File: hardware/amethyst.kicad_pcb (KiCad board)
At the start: 2 copper layers, 192 parts, among them J1 Conn_01x02_Pin, J2 USB_C_Receptacle_USB2.0_16P, SW1 SW_Push, SW10 SW_Push, SW11 SW_Push, SW12 SW_Push, SW13 SW_Push, SW14 SW_Push, SW15 SW_Push, SW16 SW_Push, SW17 SW_Push, SW18 SW_Push, SW19 SW_Push, SW2 SW_Push, SW20 SW_Push, SW21 SW_Push, SW22 SW_Push, SW23 SW_Push, SW24 SW_Push, SW25 SW_Push, SW26 SW_Push, SW27 SW_Push, SW28 SW_Push, SW29 SW_Push, SW3 SW_Push, SW30 SW_Push, SW31 SW_Push, SW32 SW_Push, SW33 SW_Push, SW34 SW_Push, SW35 SW_Push, SW36 SW_Push, SW37 SW_Push, SW38 SW_Push, SW39 SW_Push, SW4 SW_Push, SW40 SW_Push, SW41 SW_Push, SW42 SW_Push, SW43 SW_Push, SW44 SW_Push, SW45 SW_Push, SW46 SW_Push, SW47 SW_Push, SW48 SW_Push, SW49 SW_Push, SW5 SW_Push, SW50 SW_Push, SW51 SW_Push, SW52 SW_Push, SW53 SW_Push, SW54 SW_Push, SW55 SW_Push, SW56 SW_Push, SW57 SW_Push, SW58 SW_Push, SW59 SW_Push, SW6 SW_Push, SW60 SW_Push, SW61 SW_Push, SW62 SW_Push, SW63 SW_Push, SW64 SW_Push, SW65 SW_Push, SW66 SW_Push, SW67 SW_Push, SW68 SW_Push, SW69 SW_Push, SW7 SW_Push, SW70 SW_Push, SW71 SW_Push, SW72 SW_Push, SW73 SW_Push, SW74 SW_Push, SW75 SW_Push, SW76 SW_Push, SW77 SW_Push, SW78 SW_Push, SW79 SW_Push, SW8 SW_Push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

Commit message: PCB Routing
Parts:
- removed C1, C2: C, Capacitor_SMD:C_0402_1005Metric
- removed C10, C11, C12, C13, C14, C3, C4, C5, C6, C7, C8: 100n, Capacitor_SMD:C_0402_1005Metric
- removed C9: 1u, Capacitor_SMD:C_0402_1005Metric
- removed J1: Conn_01x02_Pin, Connector_PinHeader_1.00mm:PinHeader_1x02_P1.00mm_Vertical
- removed J2: USB_C_Receptacle_USB2.0_16P, Connector_USB:USB_C_Receptacle_XKB_U262-16XN-4BVC11
- removed R1, R2: 5.1k, Resistor_SMD:R_0402_1005Metric
- removed R3: 1k, Resistor_SMD:R_0402_1005Metric
- removed R4, R5: 27, Resistor_SMD:R_0402_1005Metric
- removed U1: RP2040, Package_DFN_QFN:QFN-56-1EP_7x7mm_P0.4mm_EP3.2x3.2mm
- removed U2: W25Q128JVS, Package_SO:SOIC-8_5.3x5.3mm_P1.27mm
- removed Y1: Crystal_GND24_Small, Crystal:Crystal_SMD_3225-4Pin_3.2x2.5mm
- D1, D10, D11, D12, D13, D14, D15, D16, D17, D18, D19, D2, D20, D21, D22, D23, D24, D25, D26, D27, D28, D29, D3, D30, D31, D32, D33, D34, D35, D36, D37, D38, D39, D4, D40, D41, D42, D43, D44, D45, D46, D47, D48, D49, D5, D50, D51, D52, D53, D54, D55, D56, D57, D58, D59, D6, D60, D61, D62, D63, D64, D65, D66, D67, D68, D69, D7, D70, D71, D72, D73, D74, D75, D76, D77, D78, D79, D8, D80, D81, D82, D83, D84, D9: moved to B.Cu
- moved D75 299.2 mm to (71.4, 161.9), turned to 90 degrees
- moved D17 291.3 mm to (69.1, 85.7), turned to 90 degrees
- moved D47 289.6 mm to (76.2, 123.8), turned to 90 degrees
- moved D32 289.2 mm to (73.8, 104.8), turned to 90 degrees
- moved D1 288.0 mm to (69.1, 66.7), turned to 90 degrees
- moved D61 285.1 mm to (81.0, 142.9), turned to 90 degrees
- moved D76 275.7 mm to (95.2, 161.9), turned to 90 degrees
- moved D18 274.9 mm to (88.1, 85.7), turned to 90 degrees
- moved D2 271.9 mm to (88.1, 66.7), turned to 90 degrees
- moved D33 268.0 mm to (97.6, 104.8), turned to 90 degrees
- moved D48 265.8 mm to (102.4, 123.8), turned to 90 degrees
- moved D19 258.9 mm to (107.2, 85.7), turned to 90 degrees
- moved D3 256.2 mm to (107.2, 66.7), turned to 90 degrees
- moved D62 254.9 mm to (111.9, 142.9), turned to 90 degrees
- moved D77 252.4 mm to (119.1, 161.9), turned to 90 degrees
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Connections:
- SW78 pad 1: C7 -> C6
- SW79 pad 1: C11 -> C10
- SW80 pad 1: C12 -> C11
- SW81 pad 1: C13 -> C12
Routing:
- net R2: track 0.00 -> 288.5 mm
- net R6: track 0.00 -> 287.1 mm
- net R1: track 0.00 -> 285.8 mm
- net R4: track 0.00 -> 281.3 mm
- net R3: track 0.00 -> 281.0 mm
- net R5: track 0.00 -> 275.2 mm
- net C2: track 0.00 -> 114.7 mm
- net C14: track 0.00 -> 114.3 mm
- net C3: track 0.00 -> 110.4 mm
- net C11: track 0.00 -> 107.4 mm
- net C10: track 0.00 -> 107.4 mm
- net C6: track 0.00 -> 106.3 mm
- net C1: track 0.00 -> 105.1 mm
- net C12: track 0.00 -> 103.3 mm
- net C15: track 0.00 -> 101.3 mm
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
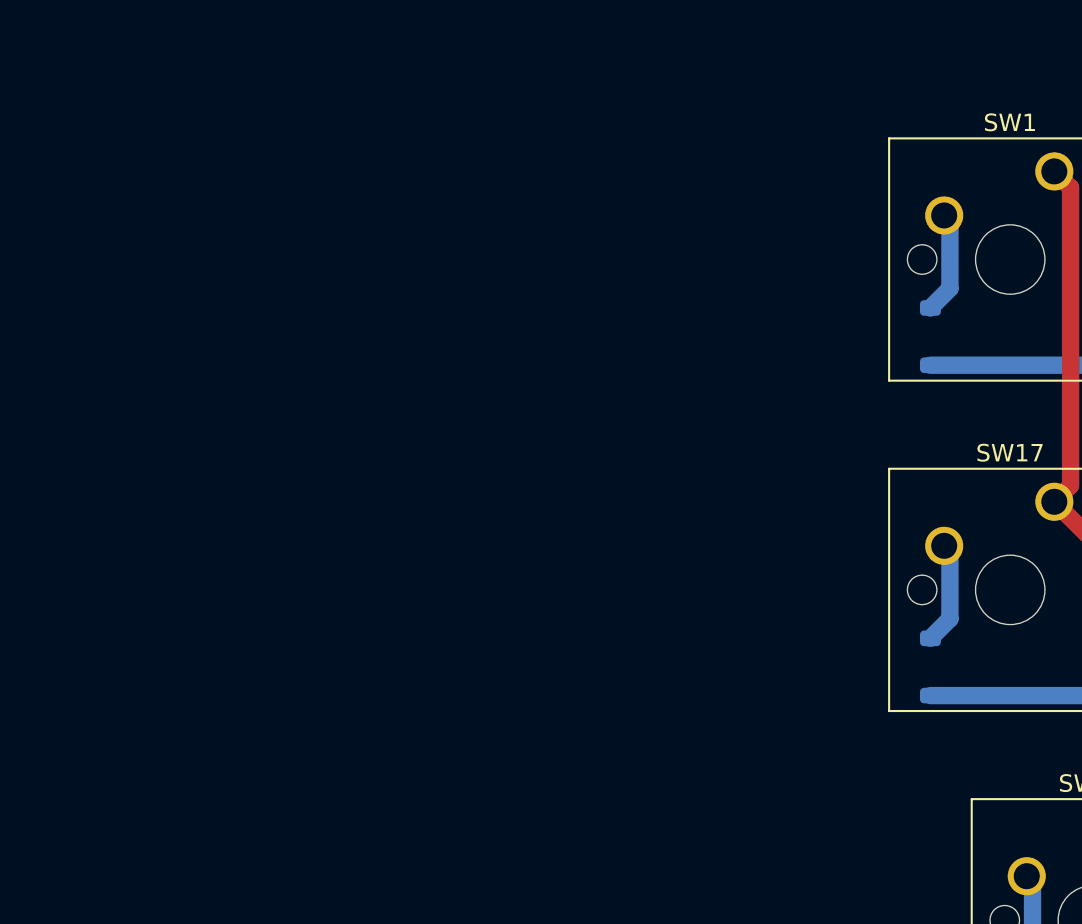
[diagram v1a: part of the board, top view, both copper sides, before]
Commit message: Power circuitry and nrf52840 circuitry
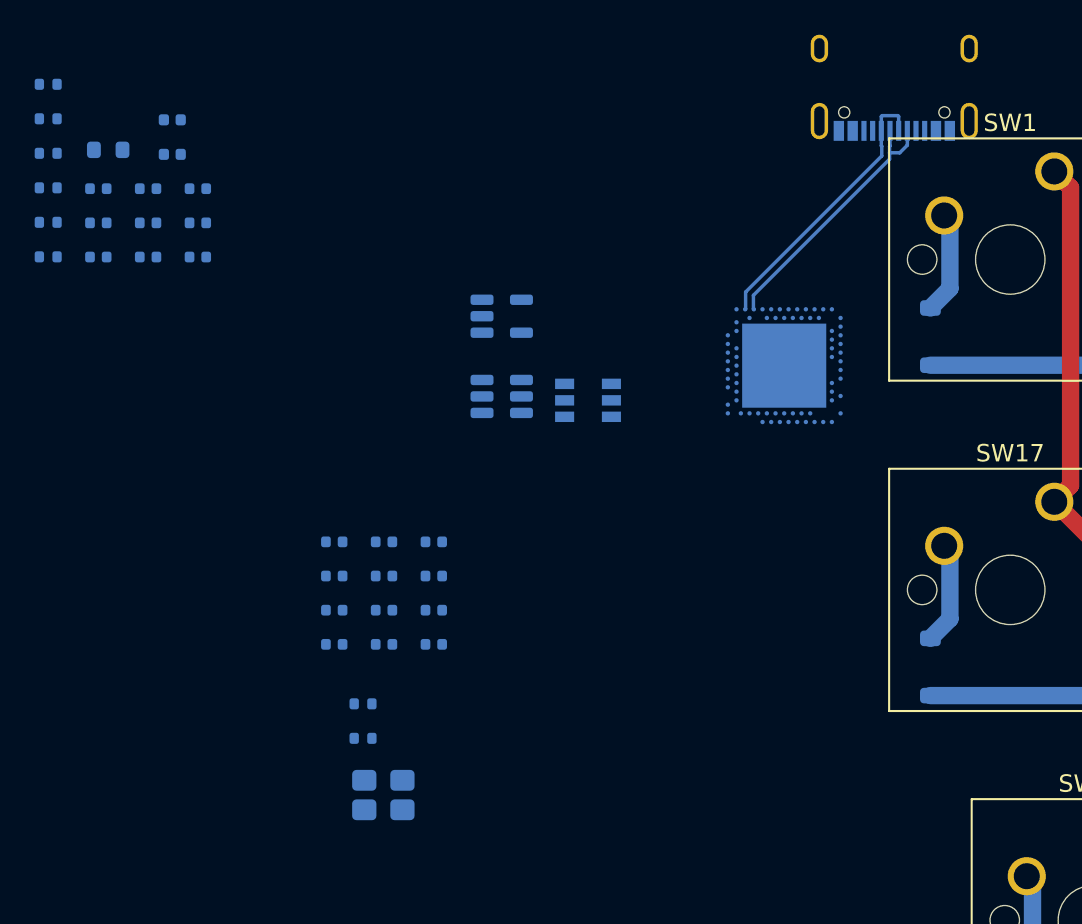
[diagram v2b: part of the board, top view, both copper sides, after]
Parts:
- added C1: C, Capacitor_SMD:C_0402_1005Metric, B.Cu at (34.7, 84.4)
- added C10: 100p, Capacitor_SMD:C_0402_1005Metric, B.Cu at (40.4, 82.5)
- added C11: 4.7u, Capacitor_SMD:C_0402_1005Metric, B.Cu at (40.4, 80.5)
- added C12: 100n, Capacitor_SMD:C_0402_1005Metric, B.Cu at (21.1, 60.1)
- added C12: 4.7u, Capacitor_SMD:C_0402_1005Metric, B.Cu at (40.4, 78.5)
- added C13: 1u, Capacitor_SMD:C_0402_1005Metric, B.Cu at (21.1, 58.1)
- added C14: 1u, Capacitor_SMD:C_0402_1005Metric, B.Cu at (23.9, 62.1)
- added C15: 47n, Capacitor_SMD:C_0402_1005Metric, B.Cu at (23.9, 60.1)
- added C16: 100n, Capacitor_SMD:C_0402_1005Metric, B.Cu at (23.9, 58.1)
- added C17: 100n, Capacitor_SMD:C_0402_1005Metric, B.Cu at (26.8, 62.1)
- added C18: 850p, Capacitor_SMD:C_0402_1005Metric, B.Cu at (26.8, 60.1)
- added C19: 100n, Capacitor_SMD:C_0402_1005Metric, B.Cu at (26.8, 58.1)
- added C2: C, Capacitor_SMD:C_0402_1005Metric, B.Cu at (34.7, 82.5)
- added C3: 100n, Capacitor_SMD:C_0402_1005Metric, B.Cu at (34.7, 80.5)
- added C4: 100n, Capacitor_SMD:C_0402_1005Metric, B.Cu at (34.7, 78.5)
- added C4: 100n, Capacitor_SMD:C_0402_1005Metric, B.Cu at (21.1, 62.1)
- added C5: 100n, Capacitor_SMD:C_0402_1005Metric, B.Cu at (37.5, 84.4)
- added C6: 100n, Capacitor_SMD:C_0402_1005Metric, B.Cu at (37.5, 82.5)
- added C7: 100n, Capacitor_SMD:C_0402_1005Metric, B.Cu at (37.5, 80.5)
- added C8: 100n, Capacitor_SMD:C_0402_1005Metric, B.Cu at (37.5, 78.5)
- added C9: 100n, Capacitor_SMD:C_0402_1005Metric, B.Cu at (40.4, 84.4)
- added D85: LED, LED_SMD:LED_0402_1005Metric, B.Cu at (25.3, 56.2)
- added D86: LED, LED_SMD:LED_0402_1005Metric, B.Cu at (25.3, 54.2)
- added FB1: FerriteBead_Small, Resistor_SMD:R_0603_1608Metric, B.Cu at (21.6, 55.9)
- added J2: USB_C_Receptacle_USB2.0_16P, Connector_USB:USB_C_Receptacle_XKB_U262-16XN-4BVC11, B.Cu at (67.0, 51.1)
- added Q1: FS8205A_C2830320, easyeda2kicad:SOT-23-6_L2.9-W1.6-P0.95-LS2.8-BR, B.Cu at (49.3, 70.3)
- added R1: 5.1k, Resistor_SMD:R_0402_1005Metric, B.Cu at (36.3, 89.8)
- added R2: 5.1k, Resistor_SMD:R_0402_1005Metric, B.Cu at (36.3, 87.8)
- added R3: 100, Resistor_SMD:R_0402_1005Metric, B.Cu at (18.2, 62.1)
- added R4: 1k, Resistor_SMD:R_0402_1005Metric, B.Cu at (18.2, 60.1)
- added R5: 1k, Resistor_SMD:R_0402_1005Metric, B.Cu at (18.2, 58.1)
- added R6: 1k, Resistor_SMD:R_0402_1005Metric, B.Cu at (18.2, 56.1)
- added R7: R, Resistor_SMD:R_0402_1005Metric, B.Cu at (18.2, 54.1)
- added R8: R, Resistor_SMD:R_0402_1005Metric, B.Cu at (18.2, 52.1)
- added U1: nRF52840, Package_DFN_QFN:Nordic_AQFN-73-1EP_7x7mm_P0.5mm, B.Cu at (60.6, 68.3)
- added U2: DW01A, Package_TO_SOT_SMD:SOT-23-6, B.Cu at (44.3, 70.1)
- added U3: MCP73831-2-OT, Package_TO_SOT_SMD:SOT-23-5, B.Cu at (44.3, 65.5)
- added Y1: Crystal_GND24_Small, Crystal:Crystal_SMD_3225-4Pin_3.2x2.5mm, B.Cu at (37.5, 93.1)
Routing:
- net D-: track 0.00 -> 16.3 mm
- net D+: track 0.00 -> 15.6 mm

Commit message: Routing
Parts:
- removed the C12 at (21.1, 60.1)
- removed the C12 at (40.4, 78.5)
- removed the C4 at (34.7, 78.5)
- removed the C4 at (21.1, 62.1)
- removed Q1: FS8205A_C2830320, easyeda2kicad:SOT-23-6_L2.9-W1.6-P0.95-LS2.8-BR
- removed R7: R, Resistor_SMD:R_0402_1005Metric
- removed U3: MCP73831-2-OT, Package_TO_SOT_SMD:SOT-23-5
- added BT1: Battery_Cell, Connector_JST:JST_EH_B2B-EH-A_1x02_P2.50mm_Vertical, B.Cu at (69.0, 98.0)
- added C12: 100n, Capacitor_SMD:C_0402_1005Metric, B.Cu at (48.2, 67.0)
- added C20: 10u, Capacitor_SMD:C_0805_2012Metric, B.Cu at (39.5, 69.9)
- added C21: 100n, Capacitor_SMD:C_0402_1005Metric, B.Cu at (42.4, 68.1)
- added C22: 1u, Capacitor_SMD:C_0402_1005Metric, B.Cu at (42.4, 66.1)
- added C23: 1u, Capacitor_SMD:C_0402_1005Metric, B.Cu at (43.9, 64.3)
- added C4: 1u, Capacitor_SMD:C_0402_1005Metric, B.Cu at (45.8, 67.3)
- C13: value 1u -> 10u; footprint Capacitor_SMD:C_0402_1005Metric -> Capacitor_SMD:C_0805_2012Metric
- D86: moved to F.Cu
- R3: value 100 -> 1k
- R4: value 1k -> 18k
- R5: value 1k -> 10k
- R6: value 1k -> R; moved to F.Cu
- U2: value DW01A -> BQ25185DLHR; footprint Package_TO_SOT_SMD:SOT-23-6 -> Package_DFN_QFN:Texas_DLH0010A_WSON-10-1EP_2.2x2mm_P0.4mm_EP0.9x1.5mm_ThermalVias
- moved R8 45.1 mm to (54.5, 78.8)
- moved R1 44.5 mm to (67.2, 57.8), turned to -90 degrees
- moved C19 43.6 mm to (65.5, 78.2), turned to 90 degrees
- moved D86 38.1 mm to (54.5, 78.8)
- moved R2 35.7 mm to (55.6, 57.8), turned to -90 degrees
- moved R5 33.8 mm to (51.8, 62.3)
- moved R4 33.7 mm to (51.8, 63.3)
- moved R3 33.6 mm to (51.8, 64.2)
- moved C15 33.1 mm to (53.5, 75.0)
- moved FB1 33.0 mm to (54.6, 55.8), turned to 180 degrees
- moved C14 32.6 mm to (53.5, 75.9)
- moved C18 32.1 mm to (54.2, 76.8)
- moved C13 32.0 mm to (53.1, 58.7)
- moved C3 31.8 mm to (65.7, 73.5), turned to 180 degrees
- moved C9 27.9 mm to (65.4, 72.1), turned to -90 degrees
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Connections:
- C13 pad 1: GND -> VBUS
- C13 pad 2: VBUS -> GND
- C16 pad 2: /VBATT -> /VSYS
- C17 pad 2: /VBATT -> /VSYS
- D85 pad 2: Net-(D85-A) -> /VSYS
- R3 pad 1: Net-(BT1-+) -> Net-(U2-ISET)
- R3 pad 2: Net-(U2-VCC) -> GND
- R4 pad 1: GND -> Net-(U2-ILIM/VSET)
- R4 pad 2: Net-(U2-CS) -> GND
- R5 pad 1: Net-(R5-Pad1) -> Net-(U2-TS/MR)
- R5 pad 2: Net-(U3-PROG) -> GND
- R6 pad 1: GND -> Net-(U2-STAT2)
- R6 pad 2: Net-(R5-Pad1) -> Net-(D85-K)
- U1 pad Y2: /VBATT -> /VSYS
- U2 pad 2: Net-(U2-CS) -> Net-(BT1-+)
- U2 pad 3: Net-(Q1-G2) -> Net-(U2-STAT2)
- U2 pad 4: unconnected-(U2-TD-Pad4) -> GND
- U2 pad 5: Net-(U2-VCC) -> GND
- U2 pad 6: Net-(BT1--) -> Net-(U2-TS/MR)
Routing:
- net D-: track 16.3 -> 0.00 mm
- net D+: track 15.6 -> 0.00 mm
- net Net-(U2-STAT2): track 0.00 -> 1.54 mm, vias 0 -> 1

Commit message: Matrix Routing and antenna placement
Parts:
- added AE1: Antenna_Chip, RF_Antenna:Johanson_2450AT18x100, F.Cu at (386.4, 75.8)
- added L1: 10u, Inductor_SMD:L_smd_1212_3232metric, B.Cu at (367.8, 80.8)
- D85: moved to F.Cu
- R6: moved to B.Cu
- moved C20 326.7 mm to (366.2, 67.0), turned to 180 degrees
- moved C21 326.0 mm to (368.4, 66.4), turned to 90 degrees
- moved D85 324.7 mm to (366.6, 62.3), turned to -90 degrees
- moved C22 324.6 mm to (367.0, 65.5)
- moved C4 324.5 mm to (370.3, 65.9)
- moved R6 324.3 mm to (366.2, 64.1), turned to -90 degrees
- moved C1 324.2 mm to (378.5, 81.4), turned to -90 degrees
- moved FB1 324.1 mm to (378.8, 52.2), turned to 0 degrees
- moved C15 323.6 mm to (377.1, 77.8), turned to 180 degrees
- moved C14 323.6 mm to (377.1, 76.9), turned to 180 degrees
- moved C23 323.3 mm to (367.1, 64.1)
- moved D86 323.2 mm to (377.6, 71.5), turned to 180 degrees
- moved R8 323.2 mm to (377.5, 71.5), turned to 180 degrees
- moved C10 322.9 mm to (377.1, 78.7), turned to 180 degrees
- moved C18 322.5 mm to (376.7, 72.9), turned to -90 degrees
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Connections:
- D85 pad 2: /VSYS -> Net-(D85-A)
- R6 pad 1: Net-(U2-STAT2) -> Net-(D85-A)
- R6 pad 2: Net-(D85-K) -> /VSYS
- U1 pad N1: unconnected-(U1-P0.08-PadN1) -> C15
- U1 pad R1: unconnected-(U1-TRACEDATA3/P1.09-PadR1) -> C16
- U1 pad U1: unconnected-(U1-TRACEDATA1/P0.12-PadU1) -> R1
- U2 pad 3: Net-(U2-STAT2) -> Net-(D85-K)
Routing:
- net Net-(C19-Pad2): track 0.00 -> 30.1 mm, vias 0 -> 5
- net VBUS: track 0.00 -> 28.5 mm, vias 0 -> 2
- net Net-(BT1-+): track 0.00 -> 28.2 mm, vias 0 -> 1
- net D+: track 0.00 -> 19.2 mm, vias 0 -> 2
- net C15: track 101.3 -> 120.0 mm, vias 0 -> 2
- net D-: track 0.00 -> 17.8 mm, vias 0 -> 2
- net R1: track 285.8 -> 301.5 mm
- net /VSYS: track 0.00 -> 9.54 mm, vias 0 -> 2
- net C16: track 95.4 -> 102.2 mm, vias 0 -> 1
- net Net-(U1-XC1): track 0.00 -> 6.73 mm
- net /DCC: track 0.00 -> 6.55 mm
- net Net-(U1-DCC): track 0.00 -> 4.42 mm
- net Net-(D85-K): track 0.00 -> 4.07 mm, vias 0 -> 1
- net Net-(U1-XC2): track 0.00 -> 4.01 mm
- net Net-(U1-DECUSB): track 0.00 -> 3.62 mm
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- added copper zone on B.Cu, net /VSYS
- added copper zone on B.Cu, net Net-(SW86-B)
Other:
- board outline added: 306.7 x 119 mm

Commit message: matrix routing
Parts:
- removed FB1: FerriteBead_Small, Resistor_SMD:R_0603_1608Metric
- moved R2 6.45 mm to (370.4, 59.2)
- moved R1 6.36 mm to (373.9, 59.2)
- moved C7 1.50 mm to (377.1, 69.5), turned to 180 degrees
- moved C6 1.47 mm to (377.1, 70.5), turned to 180 degrees
- moved C5 1.27 mm to (373.2, 68.9), turned to -135 degrees
- moved BT1 0.50 mm to (368.1, 86.5)
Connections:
- J2 pad S1: Net-(J2-SHIELD) -> unconnected-(J2-SHIELD-PadS1)
- U1 pad A10: unconnected-(U1-AIN5/P0.29-PadA10) -> C4
- U1 pad A12: unconnected-(U1-AIN0/P0.02-PadA12) -> C3
- U1 pad A8: unconnected-(U1-AIN7/P0.31-PadA8) -> R3
- U1 pad AC21: unconnected-(U1-P0.25-PadAC21) -> C5
- U1 pad AD10: unconnected-(U1-P0.15-PadAD10) -> C11
- U1 pad AD12: unconnected-(U1-P0.17-PadAD12) -> C10
- U1 pad AD16: unconnected-(U1-P0.20-PadAD16) -> C9
- U1 pad AD18: unconnected-(U1-P0.22-PadAD18) -> C8
- U1 pad AD20: unconnected-(U1-P0.24-PadAD20) -> C7
- U1 pad AD22: unconnected-(U1-TRACEDATA0/P1.00-PadAD22) -> C6
- U1 pad AD8: unconnected-(U1-P0.13-PadAD8) -> C12
- U1 pad G1: unconnected-(U1-P0.26-PadG1) -> R2
- U1 pad J1: unconnected-(U1-AIN2/P0.04-PadJ1) -> C13
- U1 pad L1: unconnected-(U1-P0.06-PadL1) -> C14
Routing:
- net C3: track 110.4 -> 378.1 mm, vias 0 -> 1
- net C5: track 86.2 -> 335.0 mm, vias 0 -> 1
- net C4: track 86.2 -> 332.0 mm, vias 0 -> 1
- net C6: track 106.3 -> 333.9 mm, vias 0 -> 1
- net C7: track 86.2 -> 293.8 mm, vias 0 -> 1
- net C8: track 86.8 -> 274.5 mm, vias 0 -> 1
- net C9: track 86.8 -> 254.5 mm, vias 0 -> 1
- net C10: track 107.4 -> 258.9 mm
- net C11: track 107.4 -> 238.9 mm
- net C12: track 103.3 -> 215.0 mm
- net C13: track 42.2 -> 107.3 mm, vias 0 -> 1
- net C14: track 114.3 -> 156.1 mm, vias 0 -> 1
- net R3: track 281.0 -> 317.1 mm
- net R2: track 288.5 -> 308.6 mm
- net /DCC: track 6.55 -> 15.3 mm, vias 0 -> 2
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
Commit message: Routing complete
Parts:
- added C24: 0.8p, Capacitor_SMD:C_0402_1005Metric, B.Cu at (376.7, 75.2)
- added C25: 0.5p, Capacitor_SMD:C_0402_1005Metric, B.Cu at (379.5, 76.1)
- added L2: 4.7n, Inductor_SMD:L_0402_1005Metric, B.Cu at (378.1, 75.7)
- added L3: 4.7n, Inductor_SMD:L_0402_1005Metric, B.Cu at (385.0, 75.1)
- added L4: 1,.8n, Inductor_SMD:L_0402_1005Metric, B.Cu at (384.1, 76.1)
- added SW85: SW_SPST, Connector_PinHeader_1.00mm:PinHeader_1x02_P1.00mm_Vertical, F.Cu at (365.2, 70.2)
- AE1: moved to B.Cu
- moved AE1 6.06 mm to (385.0, 69.9), turned to -90 degrees
- moved C8 1.45 mm to (372.4, 81.1), turned to 90 degrees
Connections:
- U1 pad A14: unconnected-(U1-P1.15-PadA14) -> R4
- U1 pad A16: unconnected-(U1-P1.13-PadA16) -> C2
- U1 pad A20: unconnected-(U1-P1.10-PadA20) -> C1
- U1 pad U24: unconnected-(U1-P1.04-PadU24) -> R6
- U1 pad W24: unconnected-(U1-P1.02-PadW24) -> R5
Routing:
- net C1: track 105.1 -> 435.9 mm, vias 0 -> 3
- net C2: track 114.7 -> 417.0 mm, vias 0 -> 1
- net R6: track 287.1 -> 394.9 mm, vias 0 -> 2
- net R5: track 275.2 -> 365.2 mm, vias 0 -> 2
- net R4: track 281.3 -> 338.1 mm
- net GND: track 3.15 -> 16.2 mm, vias 4 -> 11
- net C16: track 102.2 -> 107.0 mm
- net Net-(SW85-A): track 0.00 -> 4.00 mm
- net Net-(U1-DEC3): track 0.00 -> 3.30 mm
- net Net-(AE1-PCB_Trace): track 0.00 -> 3.30 mm
- net Net-(U1-ANT): track 0.00 -> 3.28 mm
- net Net-(C19-Pad2): track 35.0 -> 37.7 mm
- net /VSYS: track 9.54 -> 12.2 mm
- net /DCC: track 15.3 -> 14.1 mm
- net Net-(BT1-+): track 28.3 -> 29.5 mm
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- added copper zone on B.Cu, net GND
- added copper zone on F.Cu, net GND
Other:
- board size 306.7 x 119 mm -> 323.3 x 119 mm

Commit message: Antenna matching done
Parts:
- moved R5 3.84 mm to (369.7, 61.8), turned to 90 degrees
- moved R4 3.16 mm to (370.6, 61.8), turned to 90 degrees
- moved R3 2.94 mm to (371.6, 61.8), turned to 90 degrees
- moved C13 0.11 mm to (366.8, 59.1)
- moved J2 0.09 mm to (371.9, 53.3)
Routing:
- net GND: track 16.2 -> 44.6 mm, vias 11 -> 40
- net Net-(C25-Pad1): track 0.05 -> 6.83 mm
- net D-: track 18.2 -> 19.3 mm, vias 2 -> 0
- net Net-(U2-TS/MR): track 2.31 -> 1.53 mm
- net Net-(U2-ISET): track 2.27 -> 2.91 mm
- net D+: track 19.2 -> 19.0 mm, vias 2 -> 0
